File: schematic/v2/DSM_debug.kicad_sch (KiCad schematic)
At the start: 16 parts, among them J16 DSM_DBG, J20 USB_A, U33 CH340G, Y2 Crystal

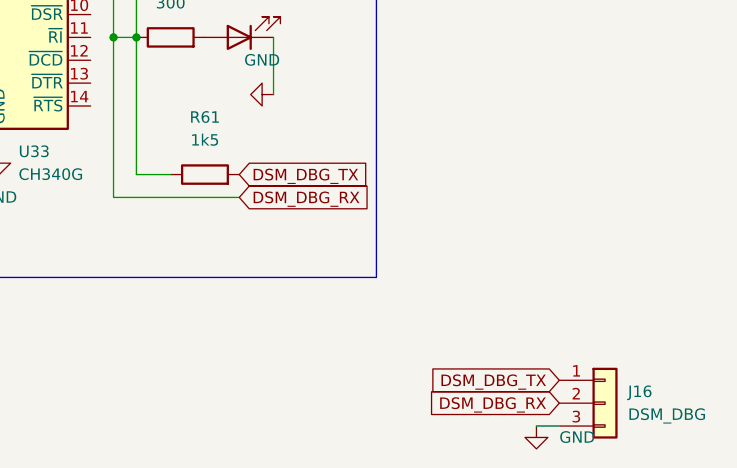
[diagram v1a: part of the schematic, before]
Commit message: v2 updates. remove sniffer
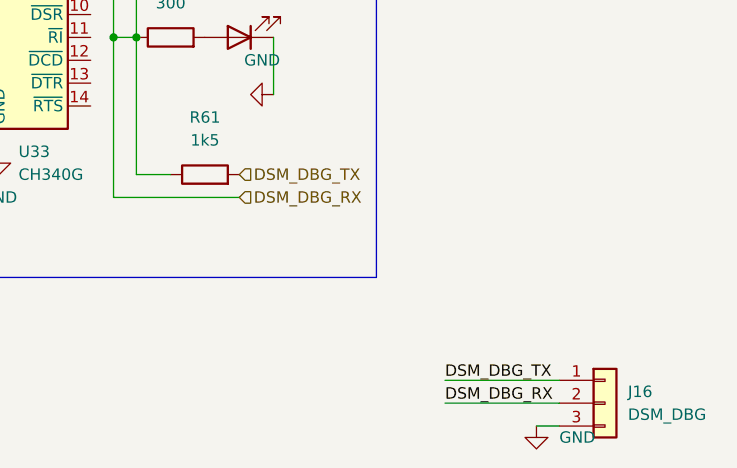
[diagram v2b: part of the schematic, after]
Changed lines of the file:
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@@
+	(wire
+		(pts
+			(xy 179.07 110.49) (xy 191.77 110.49)
+		)
+		(stroke
+			(width 0)
+			(type default)
+		)
+	)
 	(wire
 		(pts
@@
 	(wire
 		(pts
+			(xy 179.07 113.03) (xy 191.77 113.03)
+		)
+		(stroke
+			(width 0)
+			(type default)
+		)
+	)
+	(wire
+		(pts
 			(xy 144.78 87.63) (xy 148.59 87.63)
 		)
@@
 		)
 	)
-	(global_label "DSM_DBG_RX"
-		(shape input)
-		(at 191.77 113.03 180)
-		(fields_autoplaced yes)
-		(effects
-			(font
-				(size 1.27 1.27)
-			)
-			(justify right)
-		)
-		(property "Intersheetrefs" "${INTERSHEET_REFS}"
-			(at 176.6292 113.03 0)
-			(effects
-				(font
-					(size 1.27 1.27)
-				)
-				(justify right)
-				(hide yes)
-			)
-		)
-	)
-	(global_label "DSM_DBG_RX"
-		(shape input)
-		(at 156.21 90.17 0)
-		(fields_autoplaced yes)
-		(effects
-			(font
-				(size 1.27 1.27)
-			)
-			(justify left)
-		)
-		(property "Intersheetrefs" "${INTERSHEET_REFS}"
-			(at 171.0485 90.17 0)
-			(effects
-				(font
-					(size 1.27 1.27)
-				)
-				(justify left)
-				(hide yes)
-			)
+	(label "DSM_DBG_RX"
+		(at 179.07 113.03 0)
+		(effects
+			(font
+				(size 1.27 1.27)
+			)
+			(justify left bottom)
+		)
+	)
+	(label "DSM_DBG_TX"
+		(at 179.07 110.49 0)
+		(effects
+			(font
+				(size 1.27 1.27)
+			)
+			(justify left bottom)
 		)
 	)
@@
 		)
 	)
-	(global_label "DSM_DBG_TX"
-		(shape input)
-		(at 191.77 110.49 180)
-		(fields_autoplaced yes)
-		(effects
-			(font
-				(size 1.27 1.27)
-			)
-			(justify right)
-		)
-		(property "Intersheetrefs" "${INTERSHEET_REFS}"
-			(at 176.9316 110.49 0)
-			(effects
-				(font
-					(size 1.27 1.27)
-				)
-				(justify right)
-				(hide yes)
-			)
-		)
-	)
-	(global_label "DSM_DBG_TX"
-		(shape input)
-		(at 156.21 87.63 0)
-		(fields_autoplaced yes)
-		(effects
-			(font
-				(size 1.27 1.27)
-			)
-			(justify left)
-		)
-		(property "Intersheetrefs" "${INTERSHEET_REFS}"
-			(at 170.7461 87.63 0)
-			(effects
-				(font
-					(size 1.27 1.27)
-				)
-				(justify left)
-				(hide yes)
-			)
-		)
-	)
 	(global_label "DSM_VDD"
 		(shape input)
@@
 		)
 	)
+	(hierarchical_label "DSM_DBG_RX"
+		(shape input)
+		(at 156.21 90.17 0)
+		(effects
+			(font
+				(size 1.27 1.27)
+			)
+			(justify left)
+		)
+	)
+	(hierarchical_label "DSM_DBG_TX"
+		(shape input)
+		(at 156.21 87.63 0)
+		(effects
+			(font
+				(size 1.27 1.27)
+			)
+			(justify left)
+		)
+	)
